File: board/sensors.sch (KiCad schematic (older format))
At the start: 9 parts, among them J2 Molex Picoblade, Q2 Find one, U5 ELVH-100A-HANH-C-N2A5, U6 UCC2751x

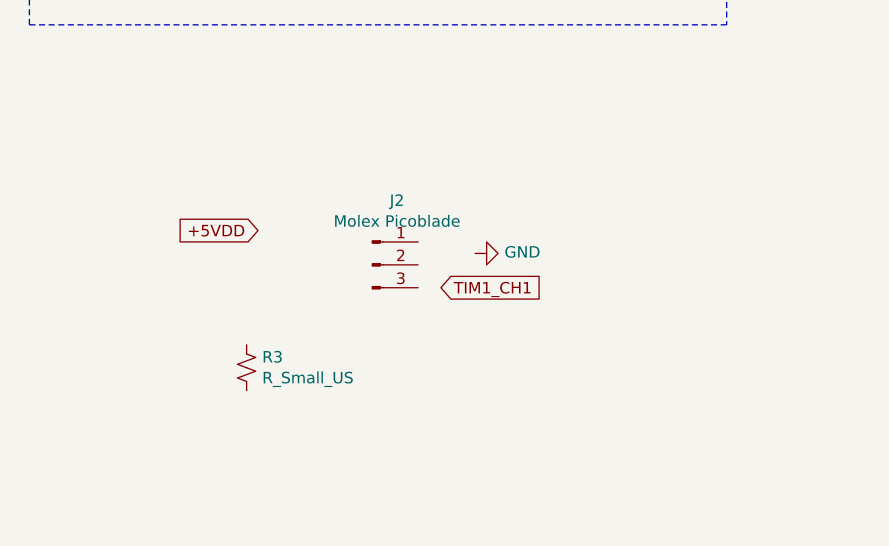
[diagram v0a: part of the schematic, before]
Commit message: Rework on power supply and added pressure sensor
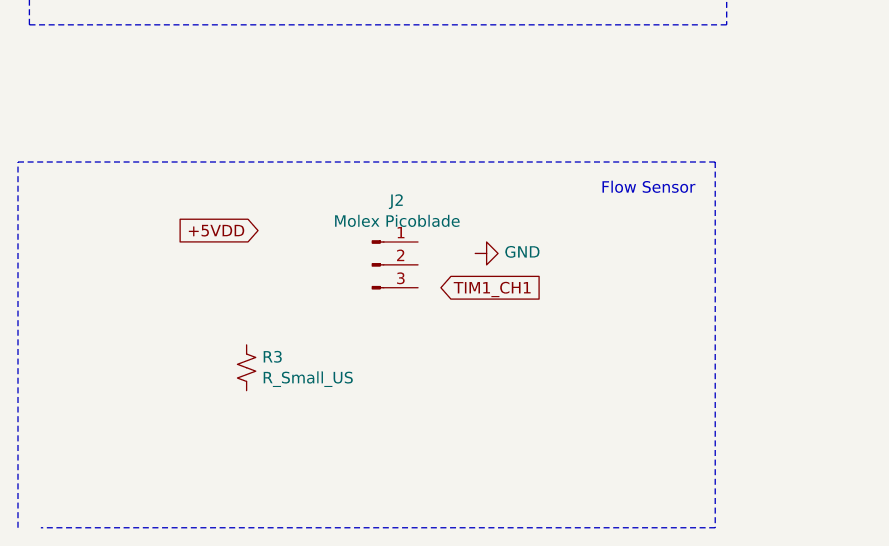
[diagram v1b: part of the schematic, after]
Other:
- note added: "Flow Sensor"
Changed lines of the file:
@@
 Wire Wire Line
 	7700 3050 7700 3150
+Wire Notes Line
+	4450 4250 4450 5850
+Wire Notes Line
+	4450 5850 1500 5850
+Wire Notes Line
+	1400 5850 1400 4250
+Wire Notes Line
+	1400 4250 4450 4250
+Text Notes 3950 4400 0    50   ~ 0
+Flow Sensor
 $EndSCHEMATC

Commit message: Update
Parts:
- renumbered C19 to C22, C20 to C23, J2 to J1, R3 to R10, R13 to R11, R2 to R12, U5 to U4, U6 to U5
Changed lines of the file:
@@
 $EndDescr
 $Comp
-L board-rescue:UCC2751x U6
+L board-rescue:UCC2751x U5
 U 1 1 609AF7D2
 P 8000 2450
-F 0 "U6" H 8025 3115 50  0000 C CNN
+F 0 "U5" H 8025 3115 50  0000 C CNN
 F 1 "UCC2751x" H 8025 3024 50  0000 C CNN
 F 2 "Package_TO_SOT_SMD:SOT-23-5" H 7950 2250 50  0001 C CNN
@@
 $EndComp
 $Comp
-L power:+12V #PWR0127
+L power:+12V #PWR035
 U 1 1 609B06A3
 P 9750 1550
-F 0 "#PWR0127" H 9750 1400 50  0001 C CNN
+F 0 "#PWR035" H 9750 1400 50  0001 C CNN
 F 1 "+12V" H 9765 1723 50  0000 C CNN
 F 2 "" H 9750 1550 50  0001 C CNN
@@
 $EndComp
 $Comp
-L Device:C_Small C19
+L Device:C_Small C22
 U 1 1 609B1116
 P 9750 1800
-F 0 "C19" H 9842 1846 50  0000 L CNN
+F 0 "C22" H 9842 1846 50  0000 L CNN
 F 1 "1u" H 9842 1755 50  0000 L CNN
 F 2 "Capacitor_SMD:C_0402_1005Metric" H 9750 1800 50  0001 C CNN
@@
 +UCC_VDD
 $Comp
-L power:GND #PWR0128
+L power:GND #PWR036
 U 1 1 609B319A
 P 9750 1950
-F 0 "#PWR0128" H 9750 1700 50  0001 C CNN
+F 0 "#PWR036" H 9750 1700 50  0001 C CNN
 F 1 "GND" H 9755 1777 50  0000 C CNN
 F 2 "" H 9750 1950 50  0001 C CNN
@@
 $EndComp
 $Comp
-L power:GND #PWR0129
+L power:GND #PWR033
 U 1 1 609B37ED
 P 7600 2200
-F 0 "#PWR0129" H 7600 1950 50  0001 C CNN
+F 0 "#PWR033" H 7600 1950 50  0001 C CNN
 F 1 "GND" V 7605 2072 50  0000 R CNN
 F 2 "" H 7600 2200 50  0001 C CNN
@@
 Connection ~ 9750 1650
 $Comp
-L Device:C_Small C20
+L Device:C_Small C23
 U 1 1 609B665A
 P 10150 1800
-F 0 "C20" H 10242 1846 50  0000 L CNN
+F 0 "C23" H 10242 1846 50  0000 L CNN
 F 1 "100n" H 10242 1755 50  0000 L CNN
 F 2 "Capacitor_SMD:C_0402_1005Metric" H 10150 1800 50  0001 C CNN
@@
 UCC_OUT
 $Comp
-L Device:R_Small_US R2
+L Device:R_Small_US R12
 U 1 1 609B7282
 P 9150 3300
-F 0 "R2" V 8945 3300 50  0000 C CNN
+F 0 "R12" V 8945 3300 50  0000 C CNN
 F 1 "100" V 9036 3300 50  0000 C CNN
 F 2 "Resistor_SMD:R_0402_1005Metric" H 9150 3300 50  0001 C CNN
@@
 	9250 3300 9450 3300
 $Comp
-L power:GND #PWR0130
+L power:GND #PWR038
 U 1 1 609B8DCD
 P 9750 3600
-F 0 "#PWR0130" H 9750 3350 50  0001 C CNN
+F 0 "#PWR038" H 9750 3350 50  0001 C CNN
 F 1 "GND" H 9755 3427 50  0000 C CNN
 F 2 "" H 9750 3600 50  0001 C CNN
@@
 	9750 2900 9800 2900
 $Comp
-L power:+12V #PWR0131
+L power:+12V #PWR037
 U 1 1 609B99FF
 P 9750 2600
-F 0 "#PWR0131" H 9750 2450 50  0001 C CNN
+F 0 "#PWR037" H 9750 2450 50  0001 C CNN
 F 1 "+12V" H 9765 2773 50  0000 C CNN
 F 2 "" H 9750 2600 50  0001 C CNN
@@
 Solenoid Driver
 $Comp
-L board-rescue:ELVH-100A-HANH-C-N2A5 U5
+L board-rescue:ELVH-100A-HANH-C-N2A5 U4
 U 1 1 609C531F
 P 2700 2550
-F 0 "U5" H 2725 3315 50  0000 C CNN
+F 0 "U4" H 2725 3315 50  0000 C CNN
 F 1 "ELVH-100A-HANH-C-N2A5" H 2725 3224 50  0000 C CNN
 F 2 "Package_DIP:DIP-8_W7.62mm_LongPads" H 2700 2550 50  0001 C CNN
@@
 SPI3_SCLK
 $Comp
-L power:GND #PWR0132
+L power:GND #PWR031
 U 1 1 609C8144
 P 2150 2200
-F 0 "#PWR0132" H 2150 1950 50  0001 C CNN
+F 0 "#PWR031" H 2150 1950 50  0001 C CNN
 F 1 "GND" H 2155 2027 50  0000 C CNN
 F 2 "" H 2150 2200 50  0001 C CNN
@@
 Pressure Sensor\n
 $Comp
-L Device:R_Small_US R3
+L Device:R_Small_US R10
 U 1 1 609D1715
 P 2400 5150
-F 0 "R3" H 2332 5104 50  0000 R CNN
+F 0 "R10" H 2332 5104 50  0000 R CNN
 F 1 "R_Small_US" H 2332 5195 50  0000 R CNN
 F 2 "Resistor_SMD:R_0402_1005Metric" H 2400 5150 50  0001 C CNN
@@
 +5VDD
 $Comp
-L Connector:Conn_01x03_Male J2
+L Connector:Conn_01x03_Male J1
 U 1 1 609DFE2E
 P 2950 4700
-F 0 "J2" H 3058 4981 50  0000 C CNN
+F 0 "J1" H 3058 4981 50  0000 C CNN
 F 1 "Molex Picoblade " H 3058 4890 50  0000 C CNN
 F 2 "Connector_Molex:Molex_PicoBlade_53047-0310_1x03_P1.25mm_Vertical" H 2950 4700 50  0001 C CNN
@@
 TIM1_CH1
 $Comp
-L power:GND #PWR012
+L power:GND #PWR032
 U 1 1 609F7F10
 P 3400 4650
-F 0 "#PWR012" H 3400 4400 50  0001 C CNN
+F 0 "#PWR032" H 3400 4400 50  0001 C CNN
 F 1 "GND" V 3405 4522 50  0000 R CNN
 F 2 "" H 3400 4650 50  0001 C CNN
@@
 UCC_EN
 $Comp
-L Device:R_Small_US R13
+L Device:R_Small_US R11
 U 1 1 609FAB86
 P 7700 3250
-F 0 "R13" H 7632 3204 50  0000 R CNN
+F 0 "R11" H 7632 3204 50  0000 R CNN
 F 1 "10k" H 7632 3295 50  0000 R CNN
 F 2 "Resistor_SMD:R_0402_1005Metric" H 7700 3250 50  0001 C CNN
@@
 	7550 3350 7700 3350
 $Comp
-L power:+12V #PWR013
+L power:+12V #PWR034
 U 1 1 609FB7AA
 P 7700 3050
-F 0 "#PWR013" H 7700 2900 50  0001 C CNN
+F 0 "#PWR034" H 7700 2900 50  0001 C CNN
 F 1 "+12V" H 7715 3223 50  0000 C CNN
 F 2 "" H 7700 3050 50  0001 C CNN

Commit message: Updated schematic
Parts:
- removed R10: R_Small_US, Resistor_SMD:R_0402_1005Metric, symbol Device:R_Small_US
- added C25, C26, C27: 100n, Capacitor_SMD:C_0402_1005Metric, symbol Device:C_Small
- added R12: 2k2, Resistor_SMD:R_0603_1608Metric, symbol Device:R_Small_US
- added R14, R15, R17: 10k, Resistor_SMD:R_0603_1608Metric, symbol Device:R_Small_US
- added U5: MX25R3235FM2xx1, Package_SO:SOP-8_5.28x5.23mm_P1.27mm, symbol Memory_Flash:MX25R3235FM2xx1
- renumbered C22 to C28, C23 to C29, Q2 to Q5, R11 to R13, R12 to R16, U4 to U3, U5 to U4
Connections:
- net labels added: +3V3, +5V, +ELVH_VDD, +FLOW_VDD, +VDD_FLASH, FLASH_!HOLD, FLASH_!WP, SPI1_!CS, SPI1_CLK, SPI1_MISO, SPI1_MOSI, SPI2_!CS, SPI2_CLK, SPI2_MISO, SPI2_MOSI, TIM2_CH3
- net labels removed: !SS_ELVH, +5VDD, ELVH_VDD, SPI3_MISO, SPI3_MOSI, SPI3_SCLK, TIM1_CH1
- wire segments 17 -> 46
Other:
- note added: "Check enable\n"
- note added: "External Flash"
- note added: "Flyback ??\n"
- note added: "Make sure of the input capture configuration\n"
- note added: "Sensors"
- moved on the sheet: C28, C29, J1, R13, R16, U3, U4

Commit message: Updated schematic
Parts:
- added C? (x3): 100n, Capacitor_SMD:C_0402_1005Metric, symbol Device:C_Small
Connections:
- net labels removed: +ELVH_VDD, +FLOW_VDD, +VDD_FLASH
- wire segments 46 -> 39
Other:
- moved on the sheet: C25, C26, C27

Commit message: Updated footprints
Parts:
- gave numbers to parts that had none: 3
- renumbered C26 to C27, C27 to C29, C28 to C31, C29 to C32
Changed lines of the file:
@@
 $EndComp
 $Comp
-L power:+12V #PWR040
+L power:+12V #PWR050
 U 1 1 609B06A3
 P 7850 1300
-F 0 "#PWR040" H 7850 1150 50  0001 C CNN
+F 0 "#PWR050" H 7850 1150 50  0001 C CNN
 F 1 "+12V" H 7865 1473 50  0000 C CNN
 F 2 "" H 7850 1300 50  0001 C CNN
@@
 $EndComp
 $Comp
-L Device:C_Small C28
+L Device:C_Small C31
 U 1 1 609B1116
 P 7850 1550
-F 0 "C28" H 7942 1596 50  0000 L CNN
+F 0 "C31" H 7942 1596 50  0000 L CNN
 F 1 "1u" H 7942 1505 50  0000 L CNN
 F 2 "Capacitor_SMD:C_0402_1005Metric" H 7850 1550 50  0001 C CNN
@@
 +UCC_VDD
 $Comp
-L power:GND #PWR041
+L power:GND #PWR051
 U 1 1 609B319A
 P 7850 1700
-F 0 "#PWR041" H 7850 1450 50  0001 C CNN
+F 0 "#PWR051" H 7850 1450 50  0001 C CNN
 F 1 "GND" H 7855 1527 50  0000 C CNN
 F 2 "" H 7850 1700 50  0001 C CNN
@@
 $EndComp
 $Comp
-L power:GND #PWR036
+L power:GND #PWR045
 U 1 1 609B37ED
 P 5850 1950
-F 0 "#PWR036" H 5850 1700 50  0001 C CNN
+F 0 "#PWR045" H 5850 1700 50  0001 C CNN
 F 1 "GND" V 5855 1822 50  0000 R CNN
 F 2 "" H 5850 1950 50  0001 C CNN
@@
 Connection ~ 7850 1400
 $Comp
-L Device:C_Small C29
+L Device:C_Small C32
 U 1 1 609B665A
 P 8250 1550
-F 0 "C29" H 8342 1596 50  0000 L CNN
+F 0 "C32" H 8342 1596 50  0000 L CNN
 F 1 "100n" H 8342 1505 50  0000 L CNN
 F 2 "Capacitor_SMD:C_0402_1005Metric" H 8250 1550 50  0001 C CNN
@@
 	7350 3050 7550 3050
 $Comp
-L power:GND #PWR043
+L power:GND #PWR053
 U 1 1 609B8DCD
 P 7850 3350
-F 0 "#PWR043" H 7850 3100 50  0001 C CNN
+F 0 "#PWR053" H 7850 3100 50  0001 C CNN
 F 1 "GND" H 7855 3177 50  0000 C CNN
 F 2 "" H 7850 3350 50  0001 C CNN
@@
 	7850 2650 7900 2650
 $Comp
-L power:+12V #PWR042
+L power:+12V #PWR052
 U 1 1 609B99FF
 P 7850 2350
-F 0 "#PWR042" H 7850 2200 50  0001 C CNN
+F 0 "#PWR052" H 7850 2200 50  0001 C CNN
 F 1 "+12V" H 7865 2523 50  0000 C CNN
 F 2 "" H 7850 2350 50  0001 C CNN
@@
 SPI1_CLK
 $Comp
-L power:GND #PWR031
+L power:GND #PWR035
 U 1 1 609C8144
 P 3300 1800
-F 0 "#PWR031" H 3300 1550 50  0001 C CNN
+F 0 "#PWR035" H 3300 1550 50  0001 C CNN
 F 1 "GND" H 3305 1627 50  0000 C CNN
 F 2 "" H 3300 1800 50  0001 C CNN
@@
 $EndComp
 $Comp
-L power:GND #PWR032
+L power:GND #PWR038
 U 1 1 609F7F10
 P 4000 3300
-F 0 "#PWR032" H 4000 3050 50  0001 C CNN
+F 0 "#PWR038" H 4000 3050 50  0001 C CNN
 F 1 "GND" V 4000 3150 50  0000 R CNN
 F 2 "" H 4000 3300 50  0001 C CNN
@@
 	5650 3100 5800 3100
 $Comp
-L power:+12V #PWR035
+L power:+12V #PWR044
 U 1 1 609FB7AA
 P 5800 2800
-F 0 "#PWR035" H 5800 2650 50  0001 C CNN
+F 0 "#PWR044" H 5800 2650 50  0001 C CNN
 F 1 "+12V" H 5815 2973 50  0000 C CNN
 F 2 "" H 5800 2800 50  0001 C CNN
@@
 Flow Sensor
 $Comp
-L power:+5V #PWR027
+L power:+5V #PWR028
 U 1 1 60B67D40
 P 2100 1400
-F 0 "#PWR027" H 2100 1250 50  0001 C CNN
+F 0 "#PWR028" H 2100 1250 50  0001 C CNN
 F 1 "+5V" H 2115 1573 50  0000 C CNN
 F 2 "" H 2100 1400 50  0001 C CNN
@@
 $EndComp
 $Comp
-L power:GND #PWR028
+L power:GND #PWR029
 U 1 1 60B6B099
 P 2100 1600
-F 0 "#PWR028" H 2100 1350 50  0001 C CNN
+F 0 "#PWR029" H 2100 1350 50  0001 C CNN
 F 1 "GND" H 2105 1427 50  0000 C CNN
 F 2 "" H 2100 1600 50  0001 C CNN
@@
 $EndComp
 $Comp
-L power:+5V #PWR029
+L power:+5V #PWR032
 U 1 1 60B6EC27
 P 2950 2800
-F 0 "#PWR029" H 2950 2650 50  0001 C CNN
+F 0 "#PWR032" H 2950 2650 50  0001 C CNN
 F 1 "+5V" H 2965 2973 50  0000 C CNN
 F 2 "" H 2950 2800 50  0001 C CNN
@@
 $EndComp
 $Comp
-L Device:C_Small C26
+L Device:C_Small C27
 U 1 1 60B6F429
 P 2950 2900
-F 0 "C26" H 3042 2946 50  0000 L CNN
+F 0 "C27" H 3042 2946 50  0000 L CNN
 F 1 "100n" H 3042 2855 50  0000 L CNN
 F 2 "Capacitor_SMD:C_0402_1005Metric" H 2950 2900 50  0001 C CNN
@@
 $EndComp
 $Comp
-L power:GND #PWR030
+L power:GND #PWR033
 U 1 1 60B6FC7B
 P 2950 3000
-F 0 "#PWR030" H 2950 2750 50  0001 C CNN
+F 0 "#PWR033" H 2950 2750 50  0001 C CNN
 F 1 "GND" H 2955 2827 50  0000 C CNN
 F 2 "" H 2950 3000 50  0001 C CNN
@@
 P 8250 5050
 AR Path="/60B9F60D" Ref="#PWR?"  Part="1"
-AR Path="/609AD7E8/60B9F60D" Ref="#PWR044"  Part="1"
-F 0 "#PWR044" H 8250 4800 50  0001 C CNN
+AR Path="/609AD7E8/60B9F60D" Ref="#PWR054"  Part="1"
+F 0 "#PWR054" H 8250 4800 50  0001 C CNN
 F 1 "GND" H 8255 4877 50  0000 C CNN
 F 2 "" H 8250 5050 50  0001 C CNN
@@
 P 6000 4150
 AR Path="/60B9F636" Ref="#PWR?"  Part="1"
-AR Path="/609AD7E8/60B9F636" Ref="#PWR037"  Part="1"
-F 0 "#PWR037" H 6000 4000 50  0001 C CNN
+AR Path="/609AD7E8/60B9F636" Ref="#PWR046"  Part="1"
+F 0 "#PWR046" H 6000 4000 50  0001 C CNN
 F 1 "+3V3" H 6015 4323 50  0000 C CNN
 F 2 "" H 6000 4150 50  0001 C CNN
@@
 P 6600 4150
 AR Path="/60B9F63C" Ref="#PWR?"  Part="1"
-AR Path="/609AD7E8/60B9F63C" Ref="#PWR038"  Part="1"
-F 0 "#PWR038" H 6600 4000 50  0001 C CNN
+AR Path="/609AD7E8/60B9F63C" Ref="#PWR047"  Part="1"
+F 0 "#PWR047" H 6600 4000 50  0001 C CNN
 F 1 "+3V3" H 6615 4323 50  0000 C CNN
 F 2 "" H 6600 4150 50  0001 C CNN
@@
 P 7800 5200
 AR Path="/60B9F65C" Ref="#PWR?"  Part="1"
-AR Path="/609AD7E8/60B9F65C" Ref="#PWR039"  Part="1"
-F 0 "#PWR039" H 7800 4950 50  0001 C CNN
+AR Path="/609AD7E8/60B9F65C" Ref="#PWR049"  Part="1"
+F 0 "#PWR049" H 7800 4950 50  0001 C CNN
 F 1 "GND" H 7805 5027 50  0000 C CNN
 F 2 "" H 7800 5200 50  0001 C CNN
@@
 P 5250 4250
 AR Path="/60B9F656" Ref="C?"  Part="1"
-AR Path="/609AD7E8/60B9F656" Ref="C27"  Part="1"
-F 0 "C27" H 5342 4296 50  0000 L CNN
+AR Path="/609AD7E8/60B9F656" Ref="C29"  Part="1"
+F 0 "C29" H 5342 4296 50  0000 L CNN
 F 1 "100n" H 5342 4205 50  0000 L CNN
 F 2 "Capacitor_SMD:C_0402_1005Metric" H 5250 4250 50  0001 C CNN
@@
 P 5250 4150
 AR Path="/60B9F650" Ref="#PWR?"  Part="1"
-AR Path="/609AD7E8/60B9F650" Ref="#PWR033"  Part="1"
-F 0 "#PWR033" H 5250 4000 50  0001 C CNN
+AR Path="/609AD7E8/60B9F650" Ref="#PWR040"  Part="1"
+F 0 "#PWR040" H 5250 4000 50  0001 C CNN
 F 1 "+3V3" H 5265 4323 50  0000 C CNN
 F 2 "" H 5250 4150 50  0001 C CNN
@@
 P 5250 4350
 AR Path="/60B9F64A" Ref="#PWR?"  Part="1"
-AR Path="/609AD7E8/60B9F64A" Ref="#PWR034"  Part="1"
-F 0 "#PWR034" H 5250 4100 50  0001 C CNN
+AR Path="/609AD7E8/60B9F64A" Ref="#PWR041"  Part="1"
+F 0 "#PWR041" H 5250 4100 50  0001 C CNN
 F 1 "GND" H 5255 4177 50  0000 C CNN
 F 2 "" H 5250 4350 50  0001 C CNN
@@
 Sensors
 $Comp
-L Device:C_Small C?
+L Device:C_Small C26
 U 1 1 60B6B891
 P 2500 1500
-F 0 "C?" H 2592 1546 50  0000 L CNN
+F 0 "C26" H 2592 1546 50  0000 L CNN
 F 1 "100n" H 2592 1455 50  0000 L CNN
 F 2 "Capacitor_SMD:C_0402_1005Metric" H 2500 1500 50  0001 C CNN
@@
 $EndComp
 $Comp
-L power:+5V #PWR?
+L power:+5V #PWR030
 U 1 1 60B74539
 P 2500 1400
-F 0 "#PWR?" H 2500 1250 50  0001 C CNN
+F 0 "#PWR030" H 2500 1250 50  0001 C CNN
 F 1 "+5V" H 2515 1573 50  0000 C CNN
 F 2 "" H 2500 1400 50  0001 C CNN
@@
 $EndComp
 $Comp
-L power:GND #PWR?
+L power:GND #PWR031
 U 1 1 60B75762
 P 2500 1600
-F 0 "#PWR?" H 2500 1350 50  0001 C CNN
+F 0 "#PWR031" H 2500 1350 50  0001 C CNN
 F 1 "GND" H 2505 1427 50  0000 C CNN
 F 2 "" H 2500 1600 50  0001 C CNN
@@
 $EndComp
 $Comp
-L power:+5V #PWR?
+L power:+5V #PWR034
 U 1 1 60B77592
 P 3250 1550
-F 0 "#PWR?" H 3250 1400 50  0001 C CNN
+F 0 "#PWR034" H 3250 1400 50  0001 C CNN
 F 1 "+5V" H 3265 1723 50  0000 C CNN
 F 2 "" H 3250 1550 50  0001 C CNN
@@
 	3250 1650 3500 1650
 $Comp
-L power:+5V #PWR?
+L power:+5V #PWR036
 U 1 1 60B78A52
 P 3350 2800
-F 0 "#PWR?" H 3350 2650 50  0001 C CNN
+F 0 "#PWR036" H 3350 2650 50  0001 C CNN
 F 1 "+5V" H 3365 2973 50  0000 C CNN
 F 2 "" H 3350 2800 50  0001 C CNN
@@
 $EndComp
 $Comp
-L Device:C_Small C?
+L Device:C_Small C28
 U 1 1 60B78ECF
 P 3350 2900
-F 0 "C?" H 3442 2946 50  0000 L CNN
+F 0 "C28" H 3442 2946 50  0000 L CNN
 F 1 "100n" H 3442 2855 50  0000 L CNN
 F 2 "Capacitor_SMD:C_0402_1005Metric" H 3350 2900 50  0001 C CNN
@@
 $EndComp
 $Comp
-L power:GND #PWR?
+L power:GND #PWR037
 U 1 1 60B7916A
 P 3350 3000
-F 0 "#PWR?" H 3350 2750 50  0001 C CNN
+F 0 "#PWR037" H 3350 2750 50  0001 C CNN
 F 1 "GND" H 3355 2827 50  0000 C CNN
 F 2 "" H 3350 3000 50  0001 C CNN
@@
 $EndComp
 $Comp
-L power:+5V #PWR?
+L power:+5V #PWR039
 U 1 1 60B7A6BE
 P 4600 3150
-F 0 "#PWR?" H 4600 3000 50  0001 C CNN
+F 0 "#PWR039" H 4600 3000 50  0001 C CNN
 F 1 "+5V" H 4615 3323 50  0000 C CNN
 F 2 "" H 4600 3150 50  0001 C CNN
@@
 P 5600 4150
 AR Path="/60B7E385" Ref="#PWR?"  Part="1"
-AR Path="/609AD7E8/60B7E385" Ref="#PWR?"  Part="1"
-F 0 "#PWR?" H 5600 4000 50  0001 C CNN
+AR Path="/609AD7E8/60B7E385" Ref="#PWR042"  Part="1"
+F 0 "#PWR042" H 5600 4000 50  0001 C CNN
 F 1 "+3V3" H 5615 4323 50  0000 C CNN
 F 2 "" H 5600 4150 50  0001 C CNN
@@
 P 5600 4250
 AR Path="/60B7E732" Ref="C?"  Part="1"
-AR Path="/609AD7E8/60B7E732" Ref="C?"  Part="1"
-F 0 "C?" H 5692 4296 50  0000 L CNN
+AR Path="/609AD7E8/60B7E732" Ref="C30"  Part="1"
+F 0 "C30" H 5692 4296 50  0000 L CNN
 F 1 "100n" H 5692 4205 50  0000 L CNN
 F 2 "Capacitor_SMD:C_0402_1005Metric" H 5600 4250 50  0001 C CNN
@@
 P 5600 4350
 AR Path="/60B7E9E5" Ref="#PWR?"  Part="1"
-AR Path="/609AD7E8/60B7E9E5" Ref="#PWR?"  Part="1"
-F 0 "#PWR?" H 5600 4100 50  0001 C CNN
+AR Path="/609AD7E8/60B7E9E5" Ref="#PWR043"  Part="1"
+F 0 "#PWR043" H 5600 4100 50  0001 C CNN
 F 1 "GND" H 5605 4177 50  0000 C CNN
 F 2 "" H 5600 4350 50  0001 C CNN
@@
 P 7800 4400
 AR Path="/60B7ED54" Ref="#PWR?"  Part="1"
-AR Path="/609AD7E8/60B7ED54" Ref="#PWR?"  Part="1"
-F 0 "#PWR?" H 7800 4250 50  0001 C CNN
+AR Path="/609AD7E8/60B7ED54" Ref="#PWR048"  Part="1"
+F 0 "#PWR048" H 7800 4250 50  0001 C CNN
 F 1 "+3V3" H 7815 4573 50  0000 C CNN
 F 2 "" H 7800 4400 50  0001 C CNN

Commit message: Update
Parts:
- removed U3: ELVH-100A-HANH-C-N2A5, Package_DIP:DIP-8_W7.62mm_LongPads, symbol board-rescue:ELVH-100A-HANH-C-N2A5
- added J6: Conn_01x06_Male, Connector_PinHeader_2.54mm:PinHeader_1x06_P2.54mm_Vertical, symbol Connector:Conn_01x06_Male
- J1: footprint Connector_Molex:Molex_PicoBlade_53047-0310_1x03_P1.25mm_Vertical -> Connector_JST:JST_XH_B3B-XH-A_1x03_P2.50mm_Vertical
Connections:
- wire segments 39 -> 36
- no-connect marks 2 -> 0
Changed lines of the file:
@@
 Text Notes 8250 1150 0    50   ~ 0
 Solenoid Driver
-$Comp
-L board-rescue:ELVH-100A-HANH-C-N2A5 U3
-U 1 1 609C531F
-P 3850 2150
-F 0 "U3" H 3875 2915 50  0000 C CNN
-F 1 "ELVH-100A-HANH-C-N2A5" H 3875 2824 50  0000 C CNN
-F 2 "Package_DIP:DIP-8_W7.62mm_LongPads" H 3850 2150 50  0001 C CNN
-F 3 "" H 3850 2150 50  0001 C CNN
-	1    3850 2150
-	1    0    0    -1
-$EndComp
-Text GLabel 3500 2100 0    50   Input ~ 0
+Text GLabel 3750 1850 0    50   Input ~ 0
 SPI1_MISO
-Text GLabel 4250 2100 2    50   Input ~ 0
+Text GLabel 3750 1650 0    50   Input ~ 0
 SPI1_MOSI
-NoConn ~ 4250 1950
-NoConn ~ 3500 1950
-Text GLabel 4250 1800 2    50   Input ~ 0
+Text GLabel 3750 1550 0    50   Input ~ 0
 SPI1_!CS
-Text GLabel 4250 1650 2    50   Input ~ 0
+Text GLabel 3750 1750 0    50   Input ~ 0
 SPI1_CLK
 $Comp
 L power:GND #PWR035
 U 1 1 609C8144
-P 3300 1800
-F 0 "#PWR035" H 3300 1550 50  0001 C CNN
-F 1 "GND" H 3305 1627 50  0000 C CNN
-F 2 "" H 3300 1800 50  0001 C CNN
-F 3 "" H 3300 1800 50  0001 C CNN
-	1    3300 1800
-	1    0    0    -1
-$EndComp
-Wire Wire Line
-	3300 1800 3500 1800
+P 3750 1950
+F 0 "#PWR035" H 3750 1700 50  0001 C CNN
+F 1 "GND" H 3755 1777 50  0000 C CNN
+F 2 "" H 3750 1950 50  0001 C CNN
+F 3 "" H 3750 1950 50  0001 C CNN
+	1    3750 1950
+	1    0    0    -1
+$EndComp
 Wire Notes Line
 	1850 1050 4900 1050
@@
 F 0 "J1" H 4050 3500 50  0000 C CNN
 F 1 "Molex Picoblade " H 4000 3050 50  0000 C CNN
-F 2 "Connector_Molex:Molex_PicoBlade_53047-0310_1x03_P1.25mm_Vertical" H 3800 3300 50  0001 C CNN
+F 2 "Connector_JST:JST_XH_B3B-XH-A_1x03_P2.50mm_Vertical" H 3800 3300 50  0001 C CNN
 F 3 "~" H 3800 3300 50  0001 C CNN
 	1    3800 3300
@@
 L power:+5V #PWR034
 U 1 1 60B77592
-P 3250 1550
-F 0 "#PWR034" H 3250 1400 50  0001 C CNN
-F 1 "+5V" H 3265 1723 50  0000 C CNN
-F 2 "" H 3250 1550 50  0001 C CNN
-F 3 "" H 3250 1550 50  0001 C CNN
-	1    3250 1550
-	1    0    0    -1
-$EndComp
-Wire Wire Line
-	3250 1550 3250 1650
-Wire Wire Line
-	3250 1650 3500 1650
+P 3750 1450
+F 0 "#PWR034" H 3750 1300 50  0001 C CNN
+F 1 "+5V" H 3765 1623 50  0000 C CNN
+F 2 "" H 3750 1450 50  0001 C CNN
+F 3 "" H 3750 1450 50  0001 C CNN
+	1    3750 1450
+	1    0    0    -1
+$EndComp
 $Comp
 L power:+5V #PWR036
@@
 	1    0    0    -1
 $EndComp
+$Comp
+L Connector:Conn_01x06_Male J6
+U 1 1 60B78D57
+P 3950 1750
+F 0 "J6" H 3922 1632 50  0000 R CNN
+F 1 "Conn_01x06_Male" H 3922 1723 50  0000 R CNN
+F 2 "Connector_PinHeader_2.54mm:PinHeader_1x06_P2.54mm_Vertical" H 3950 1750 50  0001 C CNN
+F 3 "~" H 3950 1750 50  0001 C CNN
+	1    3950 1750
+	-1   0    0    1
+$EndComp
 $EndSCHEMATC

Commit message: Push
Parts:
- removed C31: 1u, Capacitor_SMD:C_0402_1005Metric, symbol Device:C_Small
- removed C32: 100n, Capacitor_SMD:C_0402_1005Metric, symbol Device:C_Small
- removed J6: Conn_01x06_Male, Connector_PinHeader_2.54mm:PinHeader_1x06_P2.54mm_Vertical, symbol Connector:Conn_01x06_Male
- removed Q5: Find one, Package_TO_SOT_SMD:SOT-23, symbol Transistor_FET:NTR2101P
- removed R16: 100, Resistor_SMD:R_0402_1005Metric, symbol Device:R_Small_US
- removed U4: UCC2751x, Package_TO_SOT_SMD:SOT-23-5, symbol board-rescue:UCC2751x
- added C23: 10u, Capacitor_SMD:C_0402_1005Metric, symbol Device:C_Small
- added D3: B5817W, Diode_SMD:D_0805_2012Metric, symbol Device:D_Small
- added D4: LED, LED_SMD:LED_0603_1608Metric, symbol Device:LED_Small_ALT
- added J9: Screw_Terminal_01x02, TerminalBlock_Phoenix:TerminalBlock_Phoenix_PT-1,5-2-5.0-H_1x02_P5.00mm_Horizontal, symbol Connector:Screw_Terminal_01x02
- added J?: Conn_02x03_Odd_Even, symbol Connector_Generic:Conn_02x03_Odd_Even
- added R6: 5k6, Resistor_SMD:R_0603_1608Metric, symbol Device:R_Small_US
- added TP2, TP4: TestPoint, TestPoint:TestPoint_Pad_D1.0mm, symbol Connector:TestPoint
- added U3: DRV104PWPR, DRV104PWPR:IC_TPS27S100BPWPR, symbol DRV104PWPR:DRV104PWPR
- C30: value 100n -> 470p
- R13: footprint Resistor_SMD:R_0402_1005Metric -> Resistor_SMD:R_0603_1608Metric
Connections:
- net labels added: CBOOT, DAC, DRVOUT, GPIO, STATUS_OK
- net labels removed: +UCC_VDD, LOAD, UCC_EN, UCC_IN, UCC_OUT
- wire segments 36 -> 46
- no-connect marks 0 -> 3
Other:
- note removed: "Check enable\n"
- note removed: "Flyback ??\n"
